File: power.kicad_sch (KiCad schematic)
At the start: 19 parts, among them J300 USB_C_Receptacle_USB2.0_16P, U300 USBLC6-2SC6, U301 TLV62569DBV, U302 SPX3819M5-L-3-3

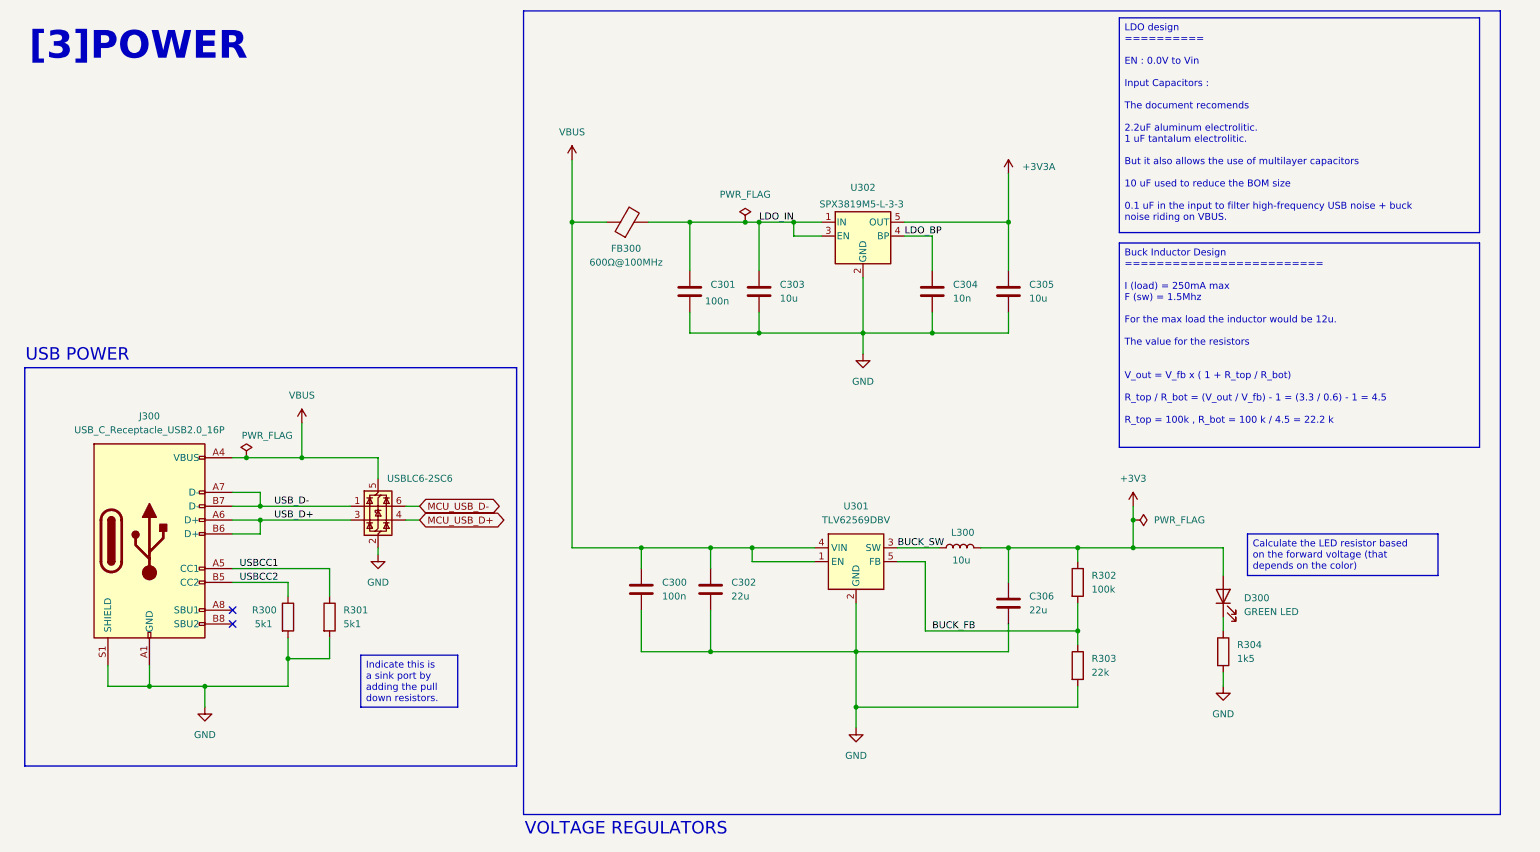
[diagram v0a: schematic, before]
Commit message: Codec updated to ES8388 on schematic
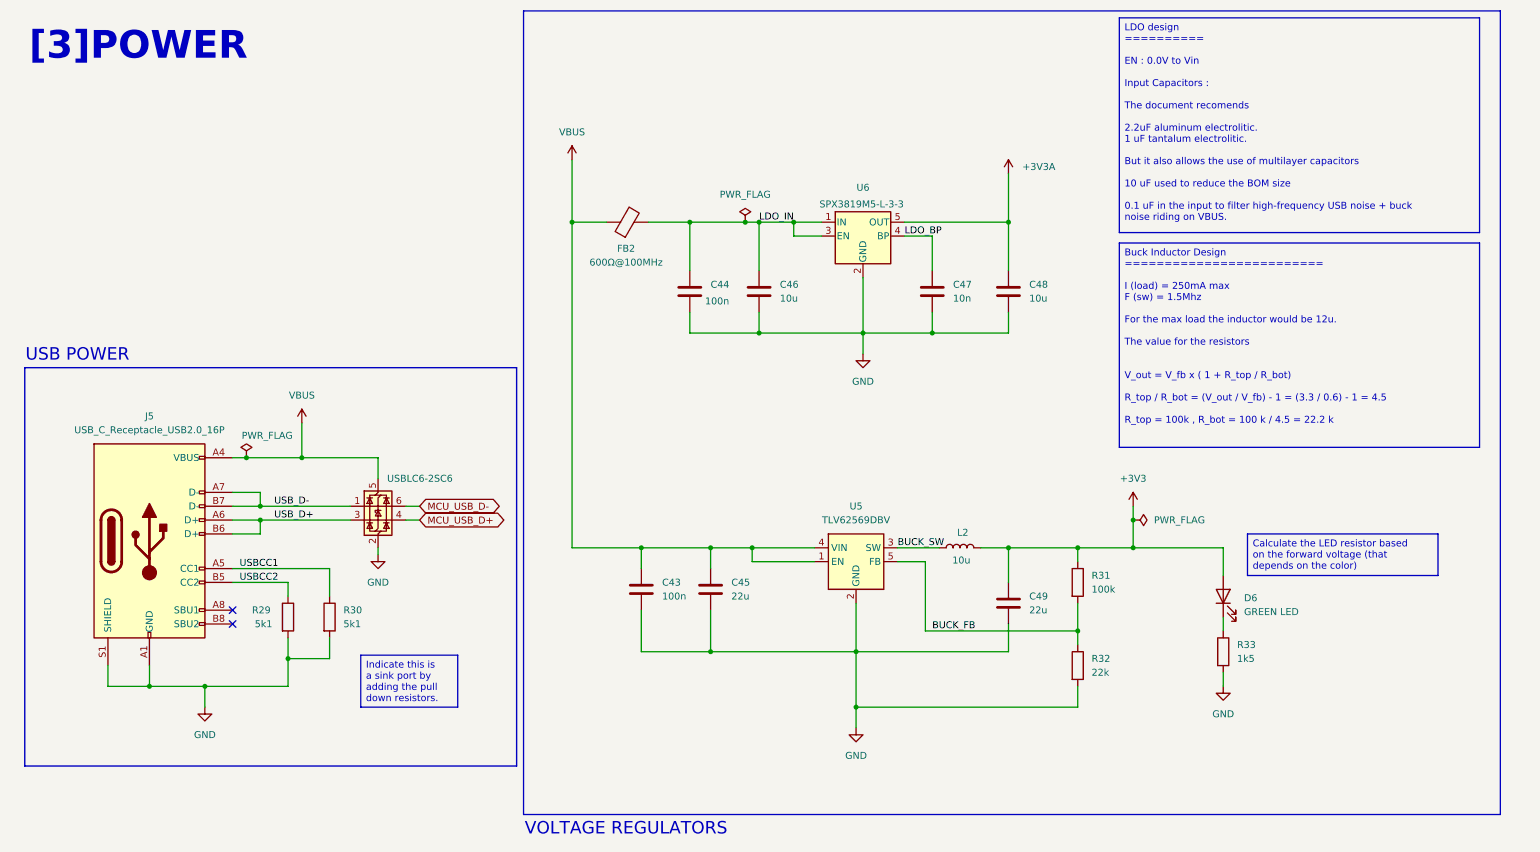
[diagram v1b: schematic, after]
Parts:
- FB2: renamed from FB300; LCSC (none) -> GZ2012D601TF
- J5: renamed from J300; LCSC (none) -> C2765186
- U4: renamed from U300; LCSC (none) -> C7519
- U5: renamed from U301; LCSC (none) -> C141836
- U6: renamed from U302; LCSC (none) -> C20617301
- renumbered C300 to C43, C301 to C44, C302 to C45, C303 to C46, C304 to C47, C305 to C48, C306 to C49, D300 to D6, L300 to L2, R300 to R29, R301 to R30, R302 to R31, R303 to R32, R304 to R33

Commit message: fillin info in parts
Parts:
- FB2: LCSC GZ2012D601TF -> (none); LCSC Part GZ2012D601TF -> C1017; Manufacturer (none) -> Sunlord; Manufacturer Part (none) -> GZ2012D601TF
- J5: LCSC C2765186 -> (none); LCSC Part (none) -> C2765186; Manufacturer (none) -> SHOU HAN; Manufacturer Part (none) -> TYPE-C 16PIN 2MD(073)
- L2: LCSC C408423 -> (none); LCSC Part (none) -> C132135; Manufacturer (none) -> SUNLORD; Manufacturer Part (none) -> MWSA0618S-100MT
- U4: LCSC C7519 -> (none); LCSC Part (none) -> C7519; Manufacturer (none) -> STMicroelectronics; Manufacturer Part (none) -> USBLC6-2SC6
- U5: LCSC C141836 -> (none); LCSC Part (none) -> C141836; Manufacturer (none) -> Texas Instruments; Manufacturer Part (none) -> TLV62569DBVR
- U6: LCSC C20617301 -> (none); LCSC Part (none) -> C20617301; Manufacturer (none) -> TECH PUBLIC; Manufacturer Part (none) -> SPX3819M5-L-3-3
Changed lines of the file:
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@@
+			)
+		)
+		(property "Manufacturer Part" ""
+			(at 233.68 121.92 90)
+			(effects
+				(font
+					(size 1.27 1.27)
+				)
+				(hide yes)
 			)
 		)
@@
 			)
 		)
+		(property "Manufacturer Part" ""
+			(at 207.01 134.62 0)
+			(effects
+				(font
+					(size 1.27 1.27)
+				)
+				(hide yes)
+			)
+		)
 		(pin "2"
 		)
@@
 			)
 		)
-		(property "LCSC" "C408423"
+		(property "LCSC Part" "C132135"
+			(at 185.42 113.03 90)
+			(effects
+				(font
+					(size 1.27 1.27)
+				)
+				(hide yes)
+			)
+		)
+		(property "Manufacturer Part" "MWSA0618S-100MT"
+			(at 185.42 113.03 90)
+			(effects
+				(font
+					(size 1.27 1.27)
+				)
+				(hide yes)
+			)
+		)
+		(property "Manufacturer" "SUNLORD"
 			(at 185.42 113.03 90)
 			(effects
@@
 			)
 		)
+		(property "Manufacturer Part" ""
+			(at 194.31 123.19 0)
+			(effects
+				(font
+					(size 1.27 1.27)
+				)
+				(hide yes)
+			)
+		)
 		(pin "2"
 		)
@@
 		)
 		(property "Description" "Resistor"
+			(at 69.85 125.73 0)
+			(effects
+				(font
+					(size 1.27 1.27)
+				)
+				(hide yes)
+			)
+		)
+		(property "Manufacturer Part" ""
 			(at 69.85 125.73 0)
 			(effects
@@
 			)
 		)
+		(property "Manufacturer Part" ""
+			(at 180.34 66.04 0)
+			(effects
+				(font
+					(size 1.27 1.27)
+				)
+				(hide yes)
+			)
+		)
 		(pin "2"
 		)
@@
 			)
 		)
+		(property "Manufacturer Part" ""
+			(at 62.23 125.73 0)
+			(effects
+				(font
+					(size 1.27 1.27)
+				)
+				(hide yes)
+			)
+		)
 		(pin "1"
 		)
@@
 			)
 		)
-		(property "LCSC" "C7519"
+		(property "LCSC Part" "C7519"
+			(at 78.74 105.41 0)
+			(effects
+				(font
+					(size 1.27 1.27)
+				)
+				(hide yes)
+			)
+		)
+		(property "Manufacturer Part" "USBLC6-2SC6"
+			(at 78.74 105.41 0)
+			(effects
+				(font
+					(size 1.27 1.27)
+				)
+				(hide yes)
+			)
+		)
+		(property "Manufacturer" "STMicroelectronics"
 			(at 78.74 105.41 0)
 			(effects
@@
 			)
 		)
-		(property "LCSC" "C20617301"
+		(property "LCSC Part" "C20617301"
+			(at 167.64 55.88 0)
+			(effects
+				(font
+					(size 1.27 1.27)
+				)
+				(hide yes)
+			)
+		)
+		(property "Manufacturer Part" "SPX3819M5-L-3-3"
+			(at 167.64 55.88 0)
+			(effects
+				(font
+					(size 1.27 1.27)
+				)
+				(hide yes)
+			)
+		)
+		(property "Manufacturer" "TECH PUBLIC"
 			(at 167.64 55.88 0)
 			(effects
@@
 			)
 		)
-		(property "LCSC" "C141836"
+		(property "LCSC Part" "C141836"
+			(at 166.37 115.57 0)
+			(effects
+				(font
+					(size 1.27 1.27)
+				)
+				(hide yes)
+			)
+		)
+		(property "Manufacturer Part" "TLV62569DBVR"
+			(at 166.37 115.57 0)
+			(effects
+				(font
+					(size 1.27 1.27)
+				)
+				(hide yes)
+			)
+		)
+		(property "Manufacturer" "Texas Instruments"
 			(at 166.37 115.57 0)
 			(effects
@@
 			)
 		)
+		(property "Manufacturer Part" ""
+			(at 127 120.65 0)
+			(effects
+				(font
+					(size 1.27 1.27)
+				)
+				(hide yes)
+			)
+		)
 		(pin "2"
 		)
@@
 			)
 		)
+		(property "Manufacturer Part" ""
+			(at 135.89 66.04 0)
+			(effects
+				(font
+					(size 1.27 1.27)
+				)
+				(hide yes)
+			)
+		)
 		(pin "2"
 		)
@@
 			)
 		)
+		(property "Manufacturer Part" ""
+			(at 139.7 120.65 0)
+			(effects
+				(font
+					(size 1.27 1.27)
+				)
+				(hide yes)
+			)
+		)
 		(pin "2"
 		)
@@
 			)
 		)
+		(property "Manufacturer Part" ""
+			(at 233.68 132.08 0)
+			(effects
+				(font
+					(size 1.27 1.27)
+				)
+				(hide yes)
+			)
+		)
 		(pin "2"
 		)
@@
 			)
 		)
-		(property "LCSC Part" "GZ2012D601TF"
+		(property "LCSC Part" "C1017"
 			(at 124.46 53.34 90)
 			(effects
@@
 			)
 		)
-		(property "LCSC" "GZ2012D601TF"
+		(property "Manufacturer Part" "GZ2012D601TF"
+			(at 124.46 53.34 90)
+			(effects
+				(font
+					(size 1.27 1.27)
+				)
+				(hide yes)
+			)
+		)
+		(property "Manufacturer" "Sunlord"
 			(at 124.46 53.34 90)
 			(effects
@@
 			)
 		)
-		(property "LCSC" "C2765186"
+		(property "LCSC Part" "C2765186"
+			(at 36.83 111.76 0)
+			(effects
+				(font
+					(size 1.27 1.27)
+				)
+				(hide yes)
+			)
+		)
+		(property "Manufacturer Part" "TYPE-C 16PIN 2MD(073)"
+			(at 36.83 111.76 0)
+			(effects
+				(font
+					(size 1.27 1.27)
+				)
+				(hide yes)
+			)
+		)
+		(property "Manufacturer" "SHOU HAN"
 			(at 36.83 111.76 0)
 			(effects
@@
 			)
 		)
+		(property "Manufacturer Part" ""
+			(at 148.59 66.04 0)
+			(effects
+				(font
+					(size 1.27 1.27)
+				)
+				(hide yes)
+			)
+		)
 		(pin "2"
 		)
@@
 			)
 		)
+		(property "Manufacturer Part" ""
+			(at 194.31 66.04 0)
+			(effects
+				(font
+					(size 1.27 1.27)
+				)
+				(hide yes)
+			)
+		)
 		(pin "2"
 		)
@@
 			(at 207.01 119.38 0)
 			(effects
+				(font
+					(size 1.27 1.27)
+				)
+				(hide yes)
+			)
+		)
+		(property "Manufacturer Part" ""
+			(at 207.01 119.38 0)
+			(effects

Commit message: JLC order
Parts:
- D6: footprint LED_SMD:LED_0402_1005Metric -> LED_SMD:LED_0805_2012Metric
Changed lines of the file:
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@@
 		)
 	)
-	(text_box "Calculate the LED resistor based on the forward voltage (that depends on the color)\n"
+	(text_box "Led current\n\nI ≈ (3.3 - 2.1) / 1.5k ≈ 0.8 mA"
 		(exclude_from_sim no)
-		(at 238.125 110.49 0)
-		(size 34.925 7.62)
+		(at 236.855 109.22 0)
+		(size 36.195 7.62)
 		(margins 0.9525 0.9525 0.9525 0.9525)
 		(stroke
@@
 			)
 		)
-		(property "Footprint" "LED_SMD:LED_0402_1005Metric"
+		(property "Footprint" "LED_SMD:LED_0805_2012Metric"
 			(at 233.68 121.92 0)
 			(effects
